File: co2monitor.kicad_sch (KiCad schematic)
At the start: 34 parts, among them J1 USB_C_Receptacle_USB2.0, J2 UART, SW1 RESET, SW2 BOOT, U1 AP2112K-3.3, U2 ESP32-S3-WROOM-1, U3 BME680, U4 SCD40, U5 74AHCT1G125

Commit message: Attempt #2
- Larger board (aesthetics)
- Add SHT30 for more accurate temperature measurements
- Larger tracks
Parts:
- added C10: 100nF, Capacitor_SMD:C_0805_2012Metric, symbol Device:C
- added D5: NeoPixel_THT, LED_SMD:LED_WS2812B_PLCC4_5.0x5.0mm_P3.2mm, symbol LED:NeoPixel_THT
- added U6: SHT30-DIS, Local:SHT30_DFN-8-1EP_2.5x2.5mm_P0.5mm_EP1.1x1.7mm, symbol Sensor_Humidity:SHT30-DIS
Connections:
- net +3V3: now also C10.2, U6.5 (VDD)
- net +5V: now also D5.3 (VDD)
- net GND: now also C10.1, D5.2 (GND), U6.2 (ADDR), U6.7 (R), U6.8 (VSS), U6.9 (VSS)
- net SCL: now also U6.4 (SCL)
- net SDA: now also U6.1 (SDA)
- net at D4.1 (DOUT): now also D5.4 (DIN)
- no-connect marks 32 -> 33

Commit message: Fix neopixel pinout/footprint
Turns out the NEOPIXEL_THT and WS2812B symbols have differing pinouts,
the WS2812B one appears to match reality, which required a slight
re-layout once the associated footprint changed.

Also fixed/enlarged a few ground tracks in the power-supply noticed
while inspecting the new area fills.

Credit to oseiler2 for spotting the pinout issue.
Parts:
- D3, D4, D5: value NeoPixel_THT -> WS2812B; symbol LED:NeoPixel_THT -> LED:WS2812B; MPN (none) -> COM-16346; Manufacturer (none) -> SparkFun Electronics
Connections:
- net +5V: now also D3.1 (VDD), D4.1 (VDD), D5.1 (VDD); no longer D3.3 (VDD), D4.3 (VDD), D5.3 (VDD)
- net GND: now also D3.3 (VSS), D4.3 (VSS), D5.3 (VSS); no longer D3.2 (GND), D4.2 (GND), D5.2 (GND)
- net at D5.4 (DIN): now also D4.2 (DOUT); no longer D4.1 (DOUT)
- net at D4.4 (DIN): now also D3.2 (DOUT); no longer D3.1 (DOUT)
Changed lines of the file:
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@@
     (pin "2")
   )
-  (symbol (lib_id "LED:NeoPixel_THT") (at 232.41 140.97 0) (unit 1)
-    (in_bom yes) (on_board yes) (fields_autoplaced)
-    (property "Reference" "D4" (id 0) (at 245.11 136.6393 0))
-    (property "Value" "NeoPixel_THT" (id 1) (at 245.11 139.1793 0))
+  (symbol (lib_id "LED:WS2812B") (at 232.41 140.97 0) (unit 1)
+    (in_bom yes) (on_board yes) (fields_autoplaced)
+    (property "Reference" "D4" (id 0) (at 243.84 136.6393 0))
+    (property "Value" "WS2812B" (id 1) (at 243.84 139.1793 0))
     (property "Footprint" "LED_SMD:LED_WS2812B_PLCC4_5.0x5.0mm_P3.2mm" (id 2) (at 233.68 148.59 0)
       (effects (font (size 1.27 1.27)) (justify left top) hide)
     )
-    (property "Datasheet" "https://www.adafruit.com/product/1938" (id 3) (at 234.95 150.495 0)
+    (property "Datasheet" "https://cdn-shop.adafruit.com/datasheets/WS2812B.pdf" (id 3) (at 234.95 150.495 0)
       (effects (font (size 1.27 1.27)) (justify left top) hide)
+    )
+    (property "Manufacturer" "SparkFun Electronics" (id 4) (at 232.41 140.97 0)
+      (effects (font (size 1.27 1.27)) hide)
+    )
+    (property "MPN" "COM-16346" (id 5) (at 232.41 140.97 0)
+      (effects (font (size 1.27 1.27)) hide)
     )
     (pin "1")
@@
     (pin "1")
   )
-  (symbol (lib_id "LED:NeoPixel_THT") (at 259.08 140.97 0) (unit 1)
-    (in_bom yes) (on_board yes) (fields_autoplaced)
-    (property "Reference" "D5" (id 0) (at 271.78 136.6393 0))
-    (property "Value" "NeoPixel_THT" (id 1) (at 271.78 139.1793 0))
+  (symbol (lib_id "LED:WS2812B") (at 259.08 140.97 0) (unit 1)
+    (in_bom yes) (on_board yes) (fields_autoplaced)
+    (property "Reference" "D5" (id 0) (at 270.51 136.6393 0))
+    (property "Value" "WS2812B" (id 1) (at 270.51 139.1793 0))
     (property "Footprint" "LED_SMD:LED_WS2812B_PLCC4_5.0x5.0mm_P3.2mm" (id 2) (at 260.35 148.59 0)
       (effects (font (size 1.27 1.27)) (justify left top) hide)
     )
-    (property "Datasheet" "https://www.adafruit.com/product/1938" (id 3) (at 261.62 150.495 0)
+    (property "Datasheet" "https://cdn-shop.adafruit.com/datasheets/WS2812B.pdf" (id 3) (at 261.62 150.495 0)
       (effects (font (size 1.27 1.27)) (justify left top) hide)
+    )
+    (property "Manufacturer" "SparkFun Electronics" (id 4) (at 259.08 140.97 0)
+      (effects (font (size 1.27 1.27)) hide)
+    )
+    (property "MPN" "COM-16346" (id 5) (at 259.08 140.97 0)
+      (effects (font (size 1.27 1.27)) hide)
     )
     (pin "1")
@@
     (pin "2")
   )
-  (symbol (lib_id "LED:NeoPixel_THT") (at 205.74 140.97 0) (unit 1)
+  (symbol (lib_id "LED:WS2812B") (at 205.74 140.97 0) (unit 1)
     (in_bom yes) (on_board yes) (fields_autoplaced)
     (property "Reference" "D3" (id 0) (at 218.44 136.6393 0))
-    (property "Value" "NeoPixel_THT" (id 1) (at 218.44 139.1793 0))
+    (property "Value" "WS2812B" (id 1) (at 218.44 139.1793 0))
     (property "Footprint" "LED_SMD:LED_WS2812B_PLCC4_5.0x5.0mm_P3.2mm" (id 2) (at 207.01 148.59 0)
       (effects (font (size 1.27 1.27)) (justify left top) hide)
     )
-    (property "Datasheet" "https://www.adafruit.com/product/1938" (id 3) (at 208.28 150.495 0)
+    (property "Datasheet" "https://cdn-shop.adafruit.com/datasheets/WS2812B.pdf" (id 3) (at 208.28 150.495 0)
       (effects (font (size 1.27 1.27)) (justify left top) hide)
+    )
+    (property "Manufacturer" "SparkFun Electronics" (id 4) (at 205.74 140.97 0)
+      (effects (font (size 1.27 1.27)) hide)
+    )
+    (property "MPN" "COM-16346" (id 5) (at 205.74 140.97 0)
+      (effects (font (size 1.27 1.27)) hide)
     )
     (pin "1")
@@
     )
     (path "/feea1fb8-0a36-4a9a-9eb4-c1983b4ae64e"
-      (reference "D3") (unit 1) (value "NeoPixel_THT") (footprint "LED_SMD:LED_WS2812B_PLCC4_5.0x5.0mm_P3.2mm")
+      (reference "D3") (unit 1) (value "WS2812B") (footprint "LED_SMD:LED_WS2812B_PLCC4_5.0x5.0mm_P3.2mm")
     )
     (path "/91b7c593-4248-4a66-91ce-f87ab80ab099"
-      (reference "D4") (unit 1) (value "NeoPixel_THT") (footprint "LED_SMD:LED_WS2812B_PLCC4_5.0x5.0mm_P3.2mm")
+      (reference "D4") (unit 1) (value "WS2812B") (footprint "LED_SMD:LED_WS2812B_PLCC4_5.0x5.0mm_P3.2mm")
     )
     (path "/d3ace197-b27f-42ab-ae6c-3a39b5610267"
-      (reference "D5") (unit 1) (value "NeoPixel_THT") (footprint "LED_SMD:LED_WS2812B_PLCC4_5.0x5.0mm_P3.2mm")
+      (reference "D5") (unit 1) (value "WS2812B") (footprint "LED_SMD:LED_WS2812B_PLCC4_5.0x5.0mm_P3.2mm")
     )
     (path "/dc3e009c-67a1-4238-b2a9-b307b1a1288c"

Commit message: Break out various signals to debugging headers
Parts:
- added J3: I2C, Connector_PinHeader_2.00mm:PinHeader_1x04_P2.00mm_Vertical, symbol Connector:Conn_01x04_Male
- added J4: 5V, Connector_PinHeader_2.00mm:PinHeader_1x02_P2.00mm_Vertical, symbol Connector:Conn_01x02_Male
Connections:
- net +3V3: now also J3.4 (Pin_4)
- net +5V: now also J4.2 (Pin_2)
- net GND: now also J3.1 (Pin_1), J4.1 (Pin_1)
- net SCL: now also J3.2 (Pin_2)
- net SDA: now also J3.3 (Pin_3)
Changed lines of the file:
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@@
+    (effects (font (size 1.27 1.27)) (justify left bottom))
+  )
+  (label "SDA" (at 45.72 154.94 0)
     (effects (font (size 1.27 1.27)) (justify left bottom))
   )
@@
   )
   (label "SCL" (at 67.31 114.3 0)
+    (effects (font (size 1.27 1.27)) (justify left bottom))
+  )
+  (label "SCL" (at 45.72 152.4 0)
     (effects (font (size 1.27 1.27)) (justify left bottom))
   )
@@
     (pin "1")
     (pin "2")
+  )
+  (symbol (lib_id "Connector:Conn_01x04_Male") (at 40.64 152.4 0) (unit 1)
+    (in_bom yes) (on_board yes)
+    (property "Reference" "J3" (id 0) (at 38.1 151.13 0))
+    (property "Value" "I2C" (id 1) (at 38.1 153.67 0))
+    (property "Footprint" "Connector_PinHeader_2.00mm:PinHeader_1x04_P2.00mm_Vertical" (id 2) (at 40.64 152.4 0)
+      (effects (font (size 1.27 1.27)) hide)
+    )
+    (property "Datasheet" "~" (id 3) (at 40.64 152.4 0)
+      (effects (font (size 1.27 1.27)) hide)
+    )
+    (pin "1")
+    (pin "2")
+    (pin "3")
+    (pin "4")
   )
   (symbol (lib_id "Mechanical:MountingHole") (at 15.24 189.23 0) (unit 1)
@@
     )
     (property "Datasheet" "" (id 3) (at 121.92 127 0)
+      (effects (font (size 1.27 1.27)) hide)
+    )
+    (pin "1")
+  )
+  (symbol (lib_id "power:GND") (at 45.72 165.1 90) (unit 1)
+    (in_bom yes) (on_board yes) (fields_autoplaced)
+    (property "Reference" "#PWR0120" (id 0) (at 52.07 165.1 0)
+      (effects (font (size 1.27 1.27)) hide)
+    )
+    (property "Value" "GND" (id 1) (at 49.53 165.0999 90)
+      (effects (font (size 1.27 1.27)) (justify right))
+    )
+    (property "Footprint" "" (id 2) (at 45.72 165.1 0)
+      (effects (font (size 1.27 1.27)) hide)
+    )
+    (property "Datasheet" "" (id 3) (at 45.72 165.1 0)
       (effects (font (size 1.27 1.27)) hide)
     )
@@
     )
     (property "Datasheet" "~" (id 3) (at 55.88 15.24 0)
+      (effects (font (size 1.27 1.27)) hide)
+    )
+    (pin "1")
+  )
+  (symbol (lib_id "power:+5V") (at 45.72 167.64 270) (unit 1)
+    (in_bom yes) (on_board yes) (fields_autoplaced)
+    (property "Reference" "#PWR0121" (id 0) (at 41.91 167.64 0)
+      (effects (font (size 1.27 1.27)) hide)
+    )
+    (property "Value" "+5V" (id 1) (at 49.53 167.6399 90)
+      (effects (font (size 1.27 1.27)) (justify left))
+    )
+    (property "Footprint" "" (id 2) (at 45.72 167.64 0)
+      (effects (font (size 1.27 1.27)) hide)
+    )
+    (property "Datasheet" "" (id 3) (at 45.72 167.64 0)
       (effects (font (size 1.27 1.27)) hide)
     )
@@
     (pin "1")
   )
+  (symbol (lib_id "power:+3.3V") (at 45.72 157.48 270) (unit 1)
+    (in_bom yes) (on_board yes) (fields_autoplaced)
+    (property "Reference" "#PWR019" (id 0) (at 41.91 157.48 0)
+      (effects (font (size 1.27 1.27)) hide)
+    )
+    (property "Value" "+3.3V" (id 1) (at 49.53 157.4799 90)
+      (effects (font (size 1.27 1.27)) (justify left))
+    )
+    (property "Footprint" "" (id 2) (at 45.72 157.48 0)
+      (effects (font (size 1.27 1.27)) hide)
+    )
+    (property "Datasheet" "" (id 3) (at 45.72 157.48 0)
+      (effects (font (size 1.27 1.27)) hide)
+    )
+    (pin "1")
+  )
   (symbol (lib_id "power:+5V") (at 184.15 134.62 0) (unit 1)
     (in_bom yes) (on_board yes) (fields_autoplaced)
@@
     )
     (property "Datasheet" "~" (id 3) (at 248.92 100.33 0)
+      (effects (font (size 1.27 1.27)) hide)
+    )
+    (pin "1")
+    (pin "2")
+  )
+  (symbol (lib_id "Connector:Conn_01x02_Male") (at 40.64 165.1 0) (unit 1)
+    (in_bom yes) (on_board yes)
+    (property "Reference" "J4" (id 0) (at 38.1 163.83 0))
+    (property "Value" "5V" (id 1) (at 38.1 166.37 0))
+    (property "Footprint" "Connector_PinHeader_2.00mm:PinHeader_1x02_P2.00mm_Vertical" (id 2) (at 40.64 165.1 0)
+      (effects (font (size 1.27 1.27)) hide)
+    )
+    (property "Datasheet" "~" (id 3) (at 40.64 165.1 0)
       (effects (font (size 1.27 1.27)) hide)
     )
@@
     )
     (property "Datasheet" "" (id 3) (at 34.29 132.08 0)
+      (effects (font (size 1.27 1.27)) hide)
+    )
+    (pin "1")
+  )
+  (symbol (lib_id "power:GND") (at 45.72 149.86 90) (unit 1)
+    (in_bom yes) (on_board yes) (fields_autoplaced)
+    (property "Reference" "#PWR018" (id 0) (at 52.07 149.86 0)
+      (effects (font (size 1.27 1.27)) hide)
+    )
+    (property "Value" "GND" (id 1) (at 49.53 149.8599 90)
+      (effects (font (size 1.27 1.27)) (justify right))
+    )
+    (property "Footprint" "" (id 2) (at 45.72 149.86 0)
+      (effects (font (size 1.27 1.27)) hide)
+    )
+    (property "Datasheet" "" (id 3) (at 45.72 149.86 0)
       (effects (font (size 1.27 1.27)) hide)
     )
@@
       (reference "#PWR017") (unit 1) (value "GND") (footprint "")
     )
+    (path "/da86a8a0-7a0a-431e-be98-42c101552521"
+      (reference "#PWR018") (unit 1) (value "GND") (footprint "")
+    )
+    (path "/b11332b0-b276-49ed-9f5e-18a396ae3354"
+      (reference "#PWR019") (unit 1) (value "+3.3V") (footprint "")
+    )
     (path "/a7fb6b96-337d-4a9d-862f-2e98673eafc4"
       (reference "#PWR0101") (unit 1) (value "GND") (footprint "")
@@
       (reference "#PWR0119") (unit 1) (value "GND") (footprint "")
     )
+    (path "/59a64ed7-6848-4851-b1b0-ed130e11a1c5"
+      (reference "#PWR0120") (unit 1) (value "GND") (footprint "")
+    )
+    (path "/61befbe2-1ff4-49a2-a20b-2b40a20959e6"
+      (reference "#PWR0121") (unit 1) (value "+5V") (footprint "")
+    )
     (path "/af9a8ac5-254c-4a31-b34a-725174ba5ffb"
       (reference "C1") (unit 1) (value "10μF") (footprint "Capacitor_SMD:C_0805_2012Metric")
@@
       (reference "J2") (unit 1) (value "UART") (footprint "Connector_PinHeader_2.00mm:PinHeader_1x02_P2.00mm_Vertical")
     )
+    (path "/4560b347-3420-4166-9ab0-99f50ae8274f"
+      (reference "J3") (unit 1) (value "I2C") (footprint "Connector_PinHeader_2.00mm:PinHeader_1x04_P2.00mm_Vertical")
+    )
+    (path "/bf860ffe-f761-47a9-8e4d-e967b9652c1b"
+      (reference "J4") (unit 1) (value "5V") (footprint "Connector_PinHeader_2.00mm:PinHeader_1x02_P2.00mm_Vertical")
+    )
     (path "/60713cde-8e76-4e1c-8936-08484f92c4ae"

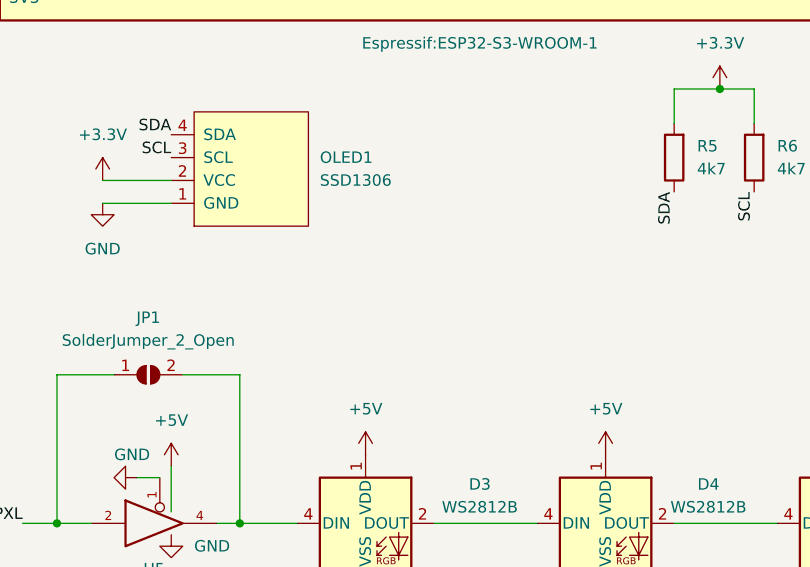
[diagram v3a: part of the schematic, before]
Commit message: Flip the screen for better positioning.
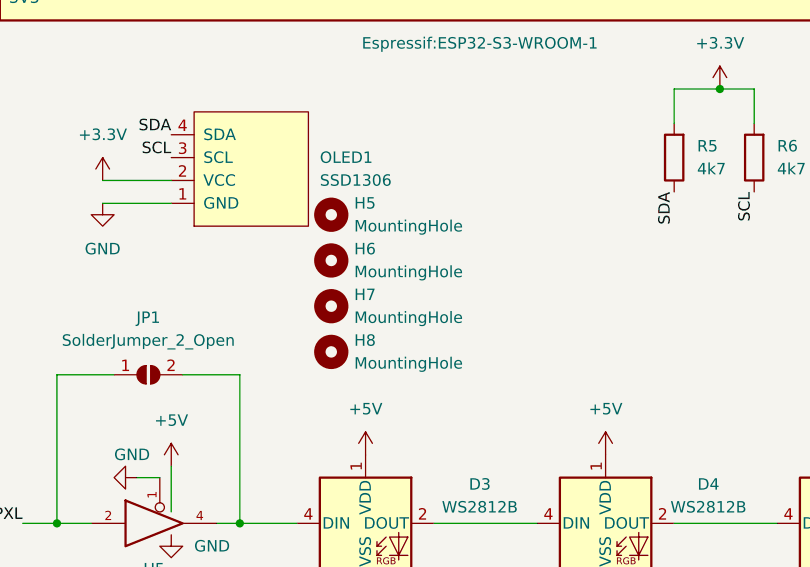
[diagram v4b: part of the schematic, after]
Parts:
- added H5, H6, H7, H8: MountingHole, MountingHole:MountingHole_2.7mm, symbol Mechanical:MountingHole
- OLED1: footprint SSD1306:128x64OLED -> SSD1306-2:OLED_128x64_0.96_small
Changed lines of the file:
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@@
+    )
+  )
+  (symbol (lib_id "Mechanical:MountingHole") (at 201.93 116.84 0) (unit 1)
+    (in_bom yes) (on_board yes) (fields_autoplaced)
+    (property "Reference" "H7" (id 0) (at 204.47 115.5699 0)
+      (effects (font (size 1.27 1.27)) (justify left))
+    )
+    (property "Value" "MountingHole" (id 1) (at 204.47 118.1099 0)
+      (effects (font (size 1.27 1.27)) (justify left))
+    )
+    (property "Footprint" "MountingHole:MountingHole_2.7mm" (id 2) (at 201.93 116.84 0)
+      (effects (font (size 1.27 1.27)) hide)
+    )
+    (property "Datasheet" "~" (id 3) (at 201.93 116.84 0)
+      (effects (font (size 1.27 1.27)) hide)
     )
   )
@@
     (pin "1")
   )
+  (symbol (lib_id "Mechanical:MountingHole") (at 201.93 111.76 0) (unit 1)
+    (in_bom yes) (on_board yes) (fields_autoplaced)
+    (property "Reference" "H6" (id 0) (at 204.47 110.4899 0)
+      (effects (font (size 1.27 1.27)) (justify left))
+    )
+    (property "Value" "MountingHole" (id 1) (at 204.47 113.0299 0)
+      (effects (font (size 1.27 1.27)) (justify left))
+    )
+    (property "Footprint" "MountingHole:MountingHole_2.7mm" (id 2) (at 201.93 111.76 0)
+      (effects (font (size 1.27 1.27)) hide)
+    )
+    (property "Datasheet" "~" (id 3) (at 201.93 111.76 0)
+      (effects (font (size 1.27 1.27)) hide)
+    )
+  )
   (symbol (lib_id "power:GND") (at 205.74 148.59 0) (unit 1)
     (in_bom yes) (on_board yes) (fields_autoplaced)
@@
     )
     (pin "1")
+  )
+  (symbol (lib_id "Mechanical:MountingHole") (at 201.93 121.92 0) (unit 1)
+    (in_bom yes) (on_board yes) (fields_autoplaced)
+    (property "Reference" "H8" (id 0) (at 204.47 120.6499 0)
+      (effects (font (size 1.27 1.27)) (justify left))
+    )
+    (property "Value" "MountingHole" (id 1) (at 204.47 123.1899 0)
+      (effects (font (size 1.27 1.27)) (justify left))
+    )
+    (property "Footprint" "MountingHole:MountingHole_2.7mm" (id 2) (at 201.93 121.92 0)
+      (effects (font (size 1.27 1.27)) hide)
+    )
+    (property "Datasheet" "~" (id 3) (at 201.93 121.92 0)
+      (effects (font (size 1.27 1.27)) hide)
+    )
   )
   (symbol (lib_id "Device:C") (at 110.49 62.23 270) (unit 1)
@@
     (pin "1")
     (pin "2")
+  )
+  (symbol (lib_id "Mechanical:MountingHole") (at 201.93 106.68 0) (unit 1)
+    (in_bom yes) (on_board yes) (fields_autoplaced)
+    (property "Reference" "H5" (id 0) (at 204.47 105.4099 0)
+      (effects (font (size 1.27 1.27)) (justify left))
+    )
+    (property "Value" "MountingHole" (id 1) (at 204.47 107.9499 0)
+      (effects (font (size 1.27 1.27)) (justify left))
+    )
+    (property "Footprint" "MountingHole:MountingHole_2.7mm" (id 2) (at 201.93 106.68 0)
+      (effects (font (size 1.27 1.27)) hide)
+    )
+    (property "Datasheet" "~" (id 3) (at 201.93 106.68 0)
+      (effects (font (size 1.27 1.27)) hide)
+    )
   )
   (symbol (lib_id "power:GND") (at 53.34 31.75 0) (unit 1)
@@
       (effects (font (size 1.27 1.27)) (justify right))
     )
-    (property "Footprint" "SSD1306:128x64OLED" (id 2) (at 186.69 101.6 0)
+    (property "Footprint" "SSD1306-2:OLED_128x64_0.96_small" (id 2) (at 186.69 101.6 0)
       (effects (font (size 1.27 1.27)) hide)
     )
@@
       (reference "H4") (unit 1) (value "MountingHole") (footprint "MountingHole:MountingHole_3.5mm")
     )
+    (path "/a3daf831-6b2f-4c2d-a1a8-61b0f1635f5c"
+      (reference "H5") (unit 1) (value "MountingHole") (footprint "MountingHole:MountingHole_2.7mm")
+    )
+    (path "/9838bd47-1c23-4649-b7ae-c2930116a0bb"
+      (reference "H6") (unit 1) (value "MountingHole") (footprint "MountingHole:MountingHole_2.7mm")
+    )
+    (path "/4a315ce3-6e1e-44fd-b749-311f9a63d813"
+      (reference "H7") (unit 1) (value "MountingHole") (footprint "MountingHole:MountingHole_2.7mm")
+    )
+    (path "/a1fa586c-885e-4bcb-a564-7b2a804264af"
+      (reference "H8") (unit 1) (value "MountingHole") (footprint "MountingHole:MountingHole_2.7mm")
+    )
     (path "/abbd7cc5-9fa9-42ab-af2d-72d337980e6e"
       (reference "J1") (unit 1) (value "USB_C_Receptacle_USB2.0") (footprint "Local:USB_C_Receptacle_XKB_U262-16XN-4BVC11")
@@
     )
     (path "/cf2f3370-b883-4939-9dc6-954c8a7fa218"
-      (reference "OLED1") (unit 1) (value "SSD1306") (footprint "SSD1306:128x64OLED")
+      (reference "OLED1") (unit 1) (value "SSD1306") (footprint "SSD1306-2:OLED_128x64_0.96_small")
     )
     (path "/8e519dd9-7824-4dae-8a17-813d3fdebec2"
